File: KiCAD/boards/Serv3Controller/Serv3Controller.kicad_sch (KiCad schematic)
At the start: 35 parts, among them J1 Conn_ARM_SWD_TagConnect_TC203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, J2 Screw_Terminal_01x02, J3 Screw_Terminal_01x02, J4 Screw_Terminal_01x02, J5 Conn_01x05, J6 Conn_01x05, U1 STM32C092FCP6, U2 SN65HVD232QDRG4Q1, U3 SST25PF020B-80-4C-SAE, U4 MAX31855KASA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

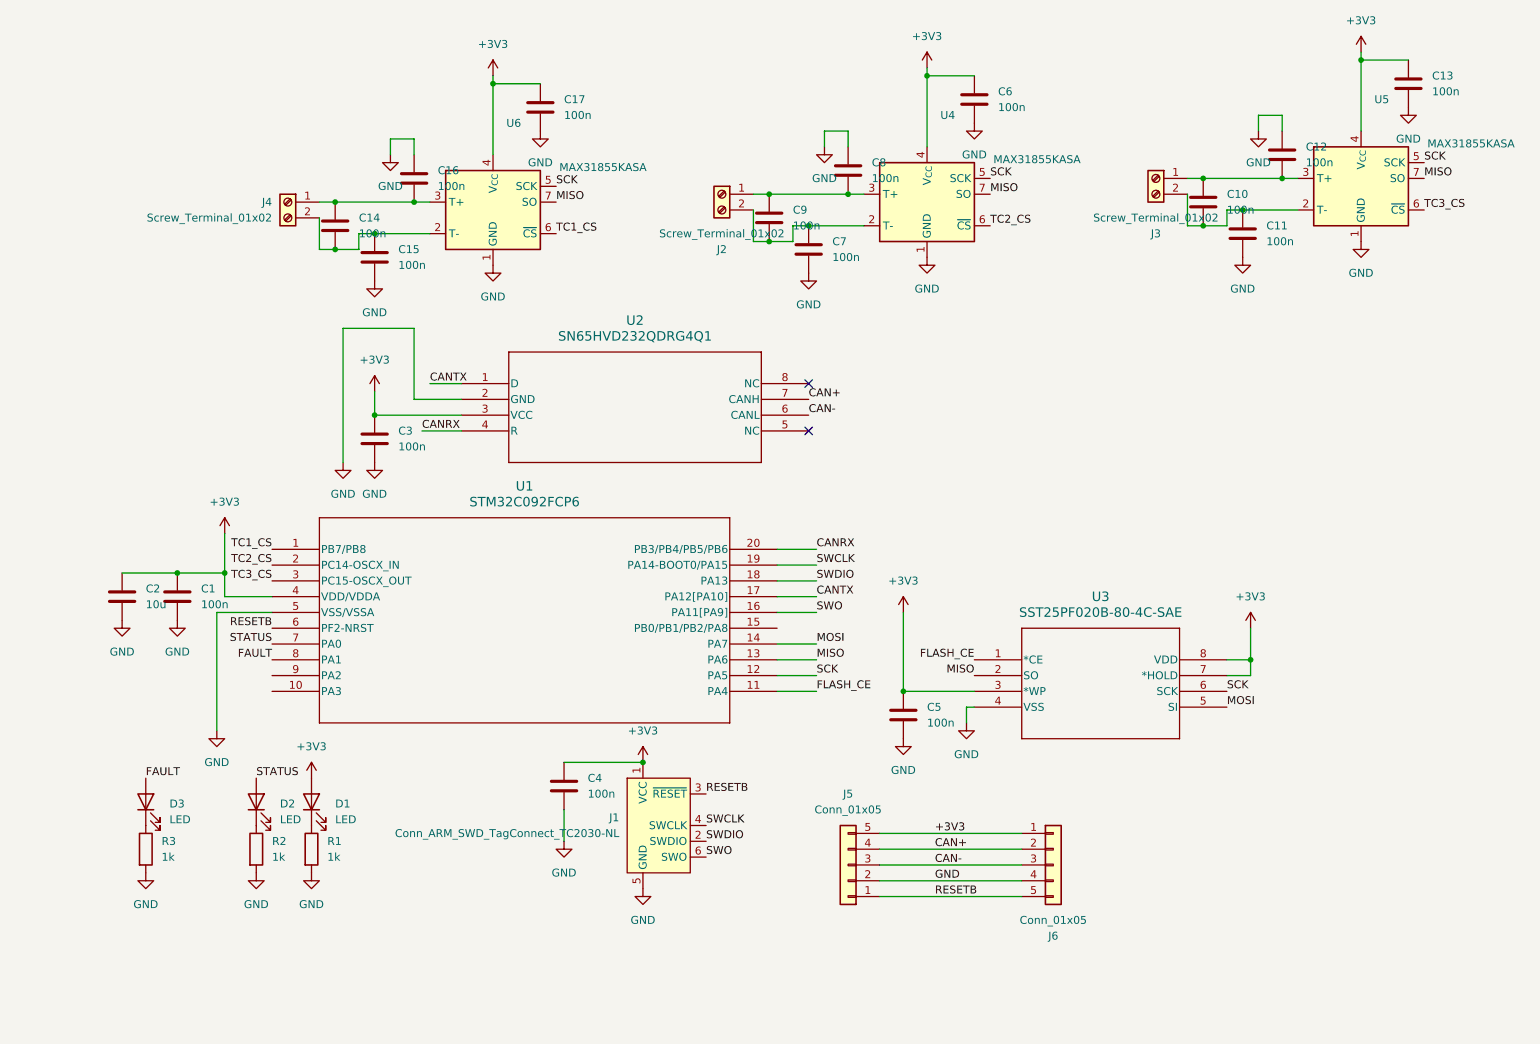
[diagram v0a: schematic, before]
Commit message: Servo controller board & fixes to TC board
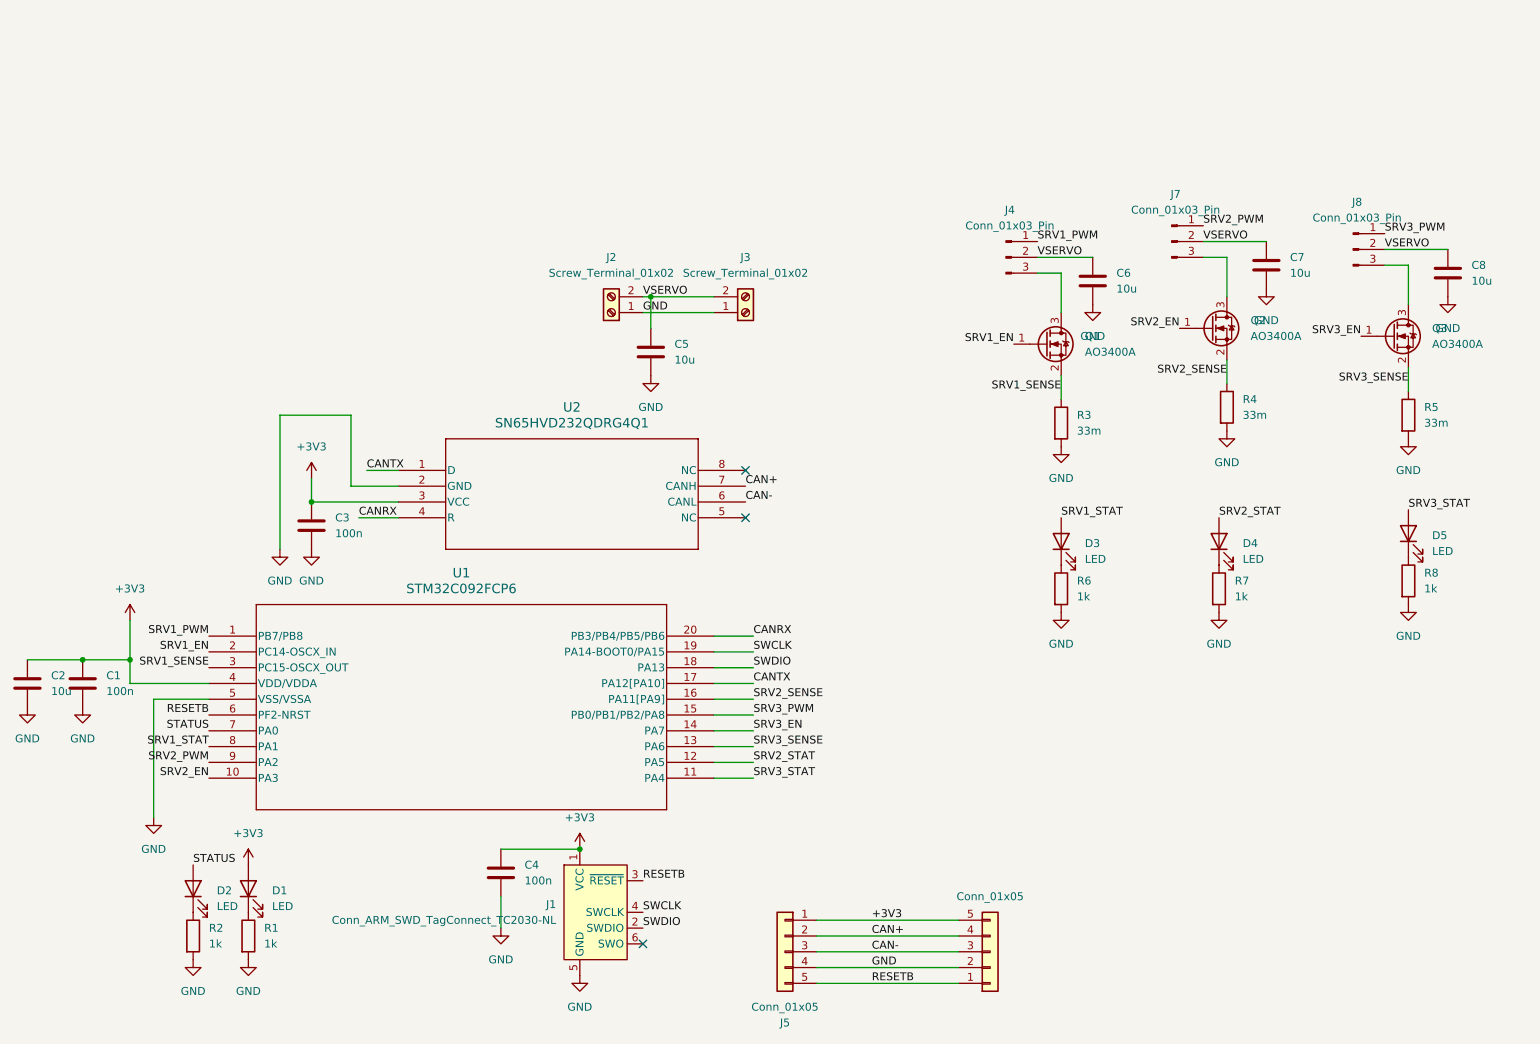
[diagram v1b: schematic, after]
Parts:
- removed C10, C11, C12, C13, C14, C15, C16, C17, C9: 100n, Capacitor_SMD:C_0603_1608Metric, symbol Device:C
- removed J4: Screw_Terminal_01x02, TerminalBlock:TerminalBlock_Xinya_XY308-2.54-2P_1x02_P2.54mm_Horizontal, symbol Connector:Screw_Terminal_01x02
- removed U3: SST25PF020B-80-4C-SAE, footprints:SOIC8_SA_SST_MCH, symbol 2025-06-11_00-53-44:SST25PF020B-80-4C-SAE
- removed U4, U5, U6: MAX31855KASA, Package_SO:SOIC-8_3.9x4.9mm_P1.27mm, symbol Sensor_Temperature:MAX31855KASA
- added D4, D5: LED, LED_SMD:LED_0603_1608Metric, symbol Device:LED
- added J4, J7, J8: Conn_01x03_Pin, Connector_PinHeader_2.54mm:PinHeader_1x03_P2.54mm_Vertical, symbol Connector:Conn_01x03_Pin
- added Q1, Q2, Q3: AO3400A, Package_TO_SOT_SMD:SOT-23, symbol Transistor_FET:AO3400A
- added R4, R5: 33m, Resistor_SMD:R_0603_1608Metric, symbol Device:R
- added R6, R7, R8: 1k, Resistor_SMD:R_0603_1608Metric, symbol Device:R
- C5, C6, C7, C8: value 100n -> 10u
- R3: value 1k -> 33m
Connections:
- net +3V3: now also J5.1 (Pin_1), J6.5 (Pin_5); no longer C5.1, C6.1, J5.5 (Pin_5), J6.1 (Pin_1)
- net CAN+: now also J5.2 (Pin_2), J6.4 (Pin_4); no longer J5.4 (Pin_4), J6.2 (Pin_2)
- net GND: now also C8.2, J2.1 (Pin_1), J3.1 (Pin_1), J5.4 (Pin_4), J6.2 (Pin_2), R4.2, R5.2, R6.2, R7.2, R8.2; no longer C8.1, J5.2 (Pin_2), J6.4 (Pin_4)
- net RESETB: now also J5.5 (Pin_5), J6.1 (Pin_1); no longer J5.1 (Pin_1), J6.5 (Pin_5)
- net at D3.1 (K): now also R6.1; no longer R3.1
- net VSERVO: now reaches C7.1, J2.2 (Pin_2)
- net VSERVO: now also C5.1, C6.1, C8.1, J3.2 (Pin_2), J4.2 (Pin_2), J7.2 (Pin_2), J8.2 (Pin_2)
- net SRV2_EN: now reaches U1.10 (PA3)
- net SRV2_EN: now also Q2.1 (G)
- net SRV3_PWM: now reaches U1.15 (PB0/PB1/PB2/PA8)
- net SRV3_PWM: now also J8.1 (Pin_1)
- net SRV2_PWM: now reaches U1.9 (PA2)
- net SRV2_PWM: now also J7.1 (Pin_1)
- net FAULT renamed SRV1_STAT
- net FLASH_CE renamed SRV3_STAT
- net SRV3_STAT: now also D5.2 (A)
- net MISO renamed SRV3_SENSE
- net SRV3_SENSE: now also Q3.2 (S), R5.1
- net MOSI renamed SRV3_EN
- net SRV3_EN: now also Q3.1 (G)
- net SCK renamed SRV2_STAT
- net SRV2_STAT: now also D4.2 (A)
- net SWO: no longer names the net of J1.6 (SWO)
- net SWO: no longer U1.16 (PA11[PA9])
- net TC1_CS renamed SRV1_PWM
- net SRV1_PWM: now also J4.1 (Pin_1)
- net TC2_CS renamed SRV1_EN
- net SRV1_EN: now also Q1.1 (G)
- net TC3_CS renamed SRV1_SENSE
- net SRV1_SENSE: now also R3.1, Q1.2 (S)
- new net: J4.3 (Pin_3), Q1.3 (D)
- new net: J7.3 (Pin_3), Q2.3 (D)
- new net: J8.3 (Pin_3), Q3.3 (D)
- new net: D5.1 (K), R8.1
- new net: D4.1 (K), R7.1
- new net SRV2_SENSE: Q2.2 (S), R4.1, U1.16 (PA11[PA9])
- no-connect marks 2 -> 3
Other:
- moved on the sheet: C1, C2, C3, C4, D1, D2, J1, J5, R1, R2, U1, U2
